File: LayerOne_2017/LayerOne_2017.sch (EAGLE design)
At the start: 102 parts, among them IC1 STM32F446_LQFP64LQFP64, IC2 REG1117, J1 SPI_TFT_DISPLAY, Q1 2N2222, Q2 MMBT2222A, U1 SN65HVD235DR, U2 SN65HVD235DR, U4 SDCARD, U5 FERRITE0805, X1 STEREOJACK, X2 MINI-USB-32005-301

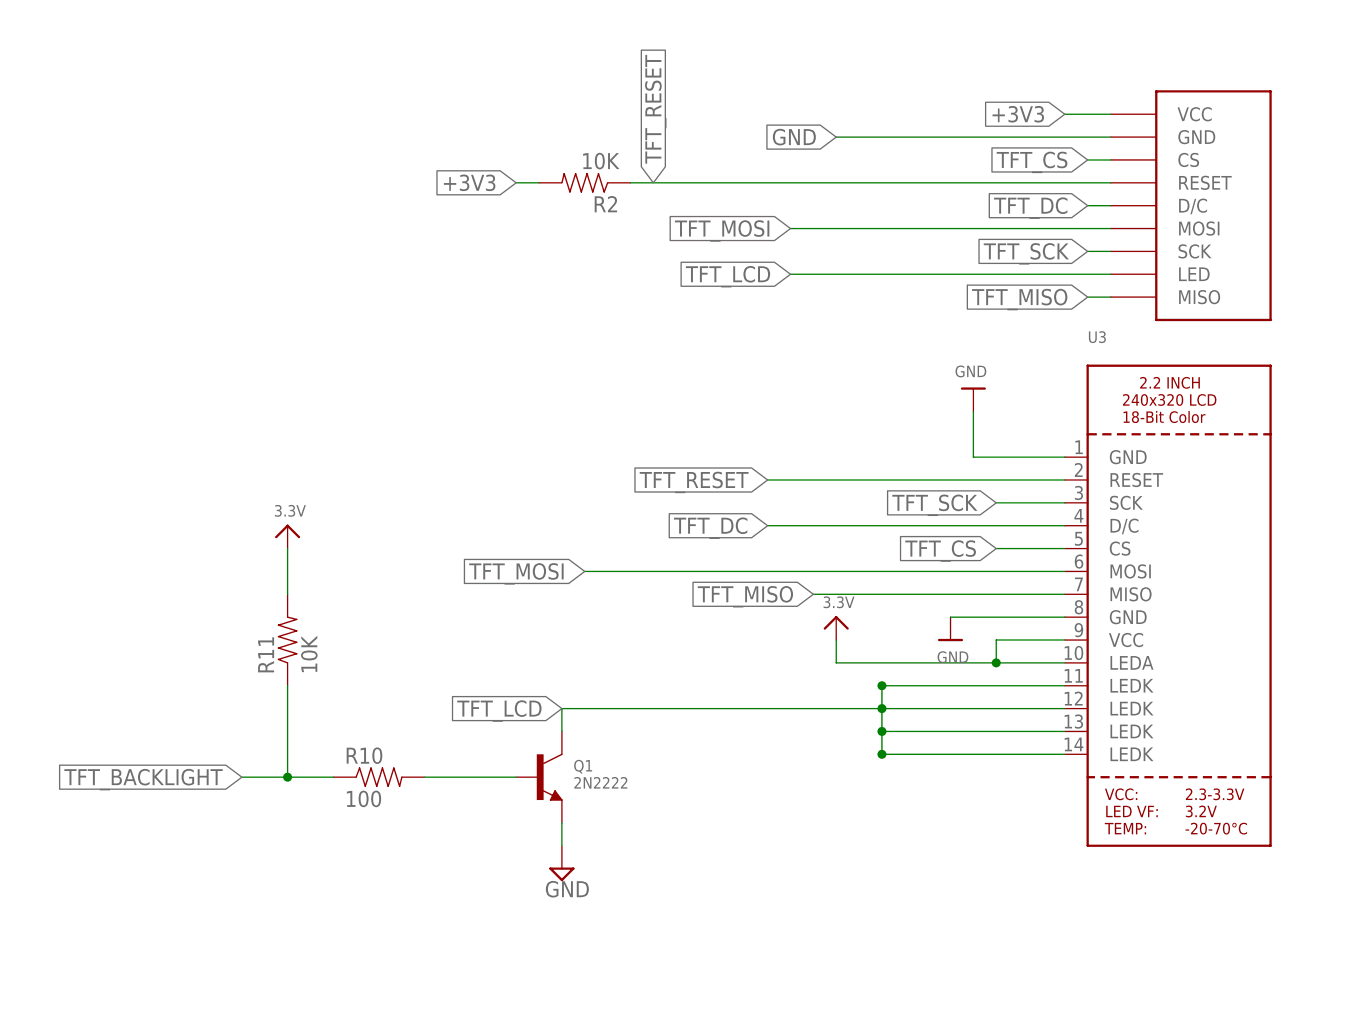
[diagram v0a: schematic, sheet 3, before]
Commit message: 
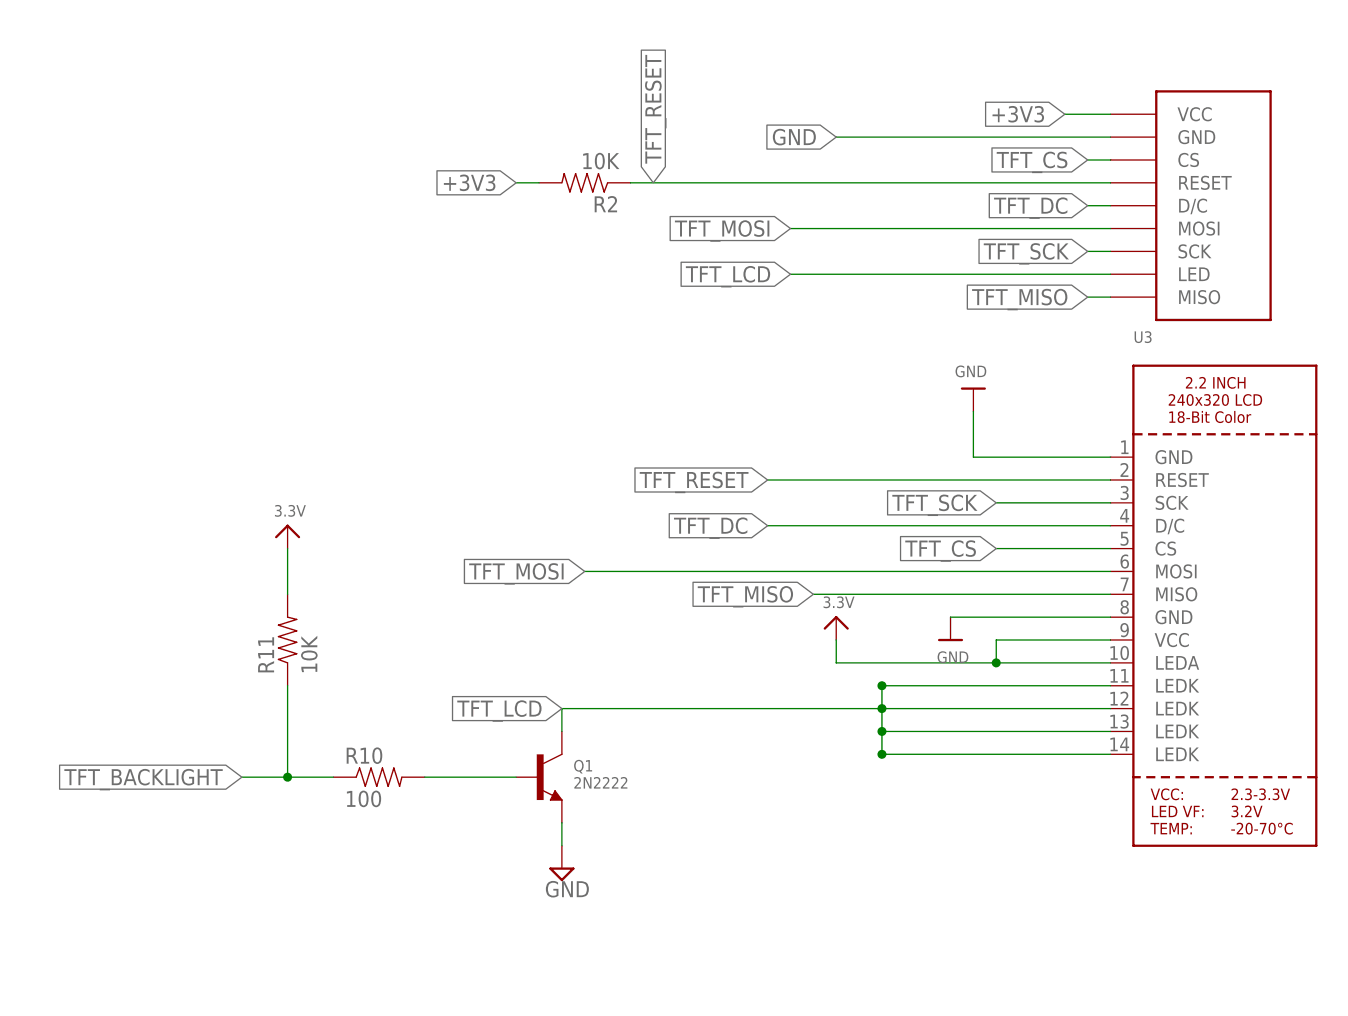
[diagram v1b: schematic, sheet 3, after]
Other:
- note removed: "Connect to MCU"
- moved on the sheet: U3
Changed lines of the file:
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@@
 <instance part="R11" gate="G$1" x="20.32" y="40.64" rot="R90"/>
 <instance part="U$21" gate="G$1" x="20.32" y="53.34"/>
-<instance part="U3" gate="G$1" x="119.38" y="43.18"/>
+<instance part="U3" gate="G$1" x="124.46" y="43.18"/>
 <instance part="U$6" gate="G$1" x="81.28" y="43.18"/>
 <instance part="U$19" gate="G$1" x="93.98" y="40.64"/>
@@
 <segment>
 <pinref part="U3" gate="G$1" pin="GND@2"/>
-<wire x1="106.68" y1="43.18" x2="93.98" y2="43.18" width="0.1524" layer="91"/>
+<wire x1="111.76" y1="43.18" x2="93.98" y2="43.18" width="0.1524" layer="91"/>
 <pinref part="U$19" gate="G$1" pin="GND"/>
 </segment>
@@
 <pinref part="U3" gate="G$1" pin="GND@1"/>
 <pinref part="U$22" gate="G$1" pin="GND"/>
-<wire x1="106.68" y1="60.96" x2="96.52" y2="60.96" width="0.1524" layer="91"/>
+<wire x1="111.76" y1="60.96" x2="96.52" y2="60.96" width="0.1524" layer="91"/>
 <wire x1="96.52" y1="60.96" x2="96.52" y2="66.04" width="0.1524" layer="91"/>
 </segment>
@@
 <pinref part="U3" gate="G$1" pin="LEDA"/>
 <pinref part="U$6" gate="G$1" pin="3.3V"/>
-<wire x1="106.68" y1="38.1" x2="99.06" y2="38.1" width="0.1524" layer="91"/>
+<wire x1="111.76" y1="38.1" x2="99.06" y2="38.1" width="0.1524" layer="91"/>
 <wire x1="99.06" y1="38.1" x2="81.28" y2="38.1" width="0.1524" layer="91"/>
 <wire x1="81.28" y1="38.1" x2="81.28" y2="40.64" width="0.1524" layer="91"/>
 <pinref part="U3" gate="G$1" pin="VCC"/>
-<wire x1="106.68" y1="40.64" x2="99.06" y2="40.64" width="0.1524" layer="91"/>
+<wire x1="111.76" y1="40.64" x2="99.06" y2="40.64" width="0.1524" layer="91"/>
 <wire x1="99.06" y1="40.64" x2="99.06" y2="38.1" width="0.1524" layer="91"/>
 <junction x="99.06" y="38.1"/>
@@
 <net name="TFT_CS" class="0">
 <segment>
-<wire x1="106.68" y1="50.8" x2="99.06" y2="50.8" width="0.1524" layer="91"/>
+<wire x1="111.76" y1="50.8" x2="99.06" y2="50.8" width="0.1524" layer="91"/>
 <label x="99.06" y="50.8" size="1.778" layer="95" rot="R180" xref="yes"/>
 <pinref part="U3" gate="G$1" pin="CS"/>
@@
 <net name="TFT_DC" class="0">
 <segment>
-<wire x1="73.66" y1="53.34" x2="106.68" y2="53.34" width="0.1524" layer="91"/>
+<wire x1="73.66" y1="53.34" x2="111.76" y2="53.34" width="0.1524" layer="91"/>
 <label x="73.66" y="53.34" size="1.778" layer="95" rot="R180" xref="yes"/>
 <pinref part="U3" gate="G$1" pin="D/C"/>
@@
 <net name="TFT_MOSI" class="0">
 <segment>
-<wire x1="106.68" y1="48.26" x2="53.34" y2="48.26" width="0.1524" layer="91"/>
+<wire x1="111.76" y1="48.26" x2="53.34" y2="48.26" width="0.1524" layer="91"/>
 <label x="53.34" y="48.26" size="1.778" layer="95" rot="R180" xref="yes"/>
 <pinref part="U3" gate="G$1" pin="MOSI"/>
@@
 <net name="TFT_SCK" class="0">
 <segment>
-<wire x1="106.68" y1="55.88" x2="99.06" y2="55.88" width="0.1524" layer="91"/>
+<wire x1="111.76" y1="55.88" x2="99.06" y2="55.88" width="0.1524" layer="91"/>
 <label x="99.06" y="55.88" size="1.778" layer="95" rot="R180" xref="yes"/>
 <pinref part="U3" gate="G$1" pin="SCK"/>
@@
 <net name="TFT_MISO" class="0">
 <segment>
-<wire x1="78.74" y1="45.72" x2="106.68" y2="45.72" width="0.1524" layer="91"/>
+<wire x1="78.74" y1="45.72" x2="111.76" y2="45.72" width="0.1524" layer="91"/>
 <label x="78.74" y="45.72" size="1.778" layer="95" rot="R180" xref="yes"/>
 <pinref part="U3" gate="G$1" pin="MISO"/>
@@
 <net name="TFT_RESET" class="0">
 <segment>
-<wire x1="106.68" y1="58.42" x2="73.66" y2="58.42" width="0.1524" layer="91"/>
+<wire x1="111.76" y1="58.42" x2="73.66" y2="58.42" width="0.1524" layer="91"/>
 <label x="73.66" y="58.42" size="1.778" layer="95" rot="R180" xref="yes"/>
 <pinref part="U3" gate="G$1" pin="RESET"/>
@@
 <pinref part="U3" gate="G$1" pin="LEDK@2"/>
 <wire x1="50.8" y1="33.02" x2="86.36" y2="33.02" width="0.1524" layer="91"/>
-<wire x1="86.36" y1="33.02" x2="106.68" y2="33.02" width="0.1524" layer="91"/>
+<wire x1="86.36" y1="33.02" x2="111.76" y2="33.02" width="0.1524" layer="91"/>
 <wire x1="86.36" y1="33.02" x2="86.36" y2="35.56" width="0.1524" layer="91"/>
 <pinref part="U3" gate="G$1" pin="LEDK@4"/>
-<wire x1="106.68" y1="27.94" x2="86.36" y2="27.94" width="0.1524" layer="91"/>
+<wire x1="111.76" y1="27.94" x2="86.36" y2="27.94" width="0.1524" layer="91"/>
 <wire x1="86.36" y1="33.02" x2="86.36" y2="30.48" width="0.1524" layer="91"/>
 <wire x1="86.36" y1="30.48" x2="86.36" y2="27.94" width="0.1524" layer="91"/>
-<wire x1="106.68" y1="30.48" x2="86.36" y2="30.48" width="0.1524" layer="91"/>
+<wire x1="111.76" y1="30.48" x2="86.36" y2="30.48" width="0.1524" layer="91"/>
 <pinref part="U3" gate="G$1" pin="LEDK@3"/>
 <junction x="86.36" y="30.48"/>
 <junction x="86.36" y="33.02"/>
-<wire x1="106.68" y1="35.56" x2="86.36" y2="35.56" width="0.1524" layer="91"/>
+<wire x1="111.76" y1="35.56" x2="86.36" y2="35.56" width="0.1524" layer="91"/>
 <pinref part="U3" gate="G$1" pin="LEDK@1"/>
 <junction x="86.36" y="35.56"/>
@@
 <sheet>
 <plain>
-<text x="93.98" y="-7.62" size="1.778" layer="91" rot="R90">Connect to MCU</text>
 </plain>
 <instances>

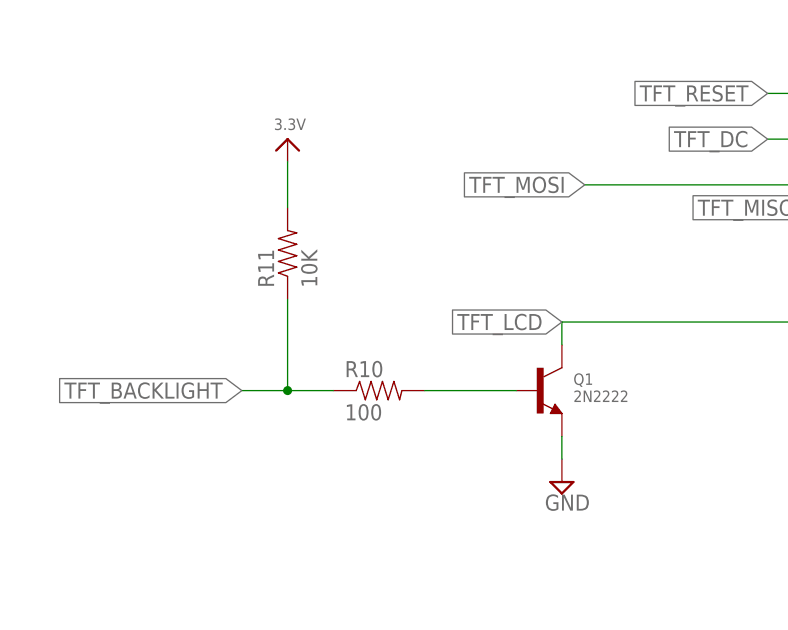
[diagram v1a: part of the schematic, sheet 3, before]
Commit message: Backlight NPN redone
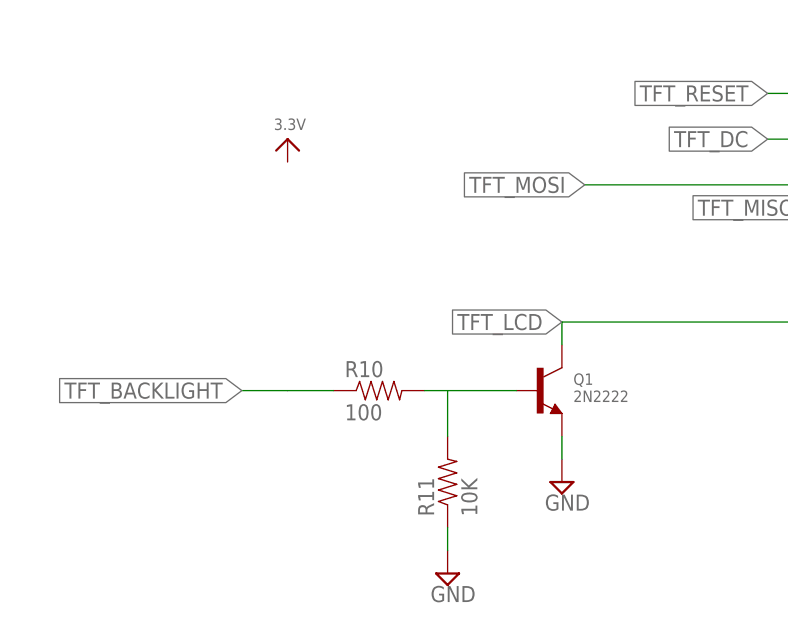
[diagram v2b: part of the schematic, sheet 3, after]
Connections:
- net +3V3: no longer R11.2
- net GND: now also R11.1
- net N$16: now also R11.2
- net TFT_BACKLIGHT: no longer R11.1
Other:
- moved on the sheet: R11
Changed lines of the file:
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@@
 </part>
 <part name="U$43" library="microbuilder" deviceset="GND" device=""/>
+<part name="GND2" library="STM32-PROX" deviceset="GND" device=""/>
 </parts>
 <sheets>
@@
 <instance part="Q1" gate="G$1" x="50.8" y="25.4"/>
 <instance part="R10" gate="G$1" x="30.48" y="25.4"/>
-<instance part="R11" gate="G$1" x="20.32" y="40.64" rot="R90"/>
+<instance part="R11" gate="G$1" x="38.1" y="15.24" rot="R90"/>
 <instance part="U$21" gate="G$1" x="20.32" y="53.34"/>
 <instance part="U3" gate="G$1" x="124.46" y="43.18"/>
@@
 <attribute name="DIGIKEY" x="53.34" y="91.44" size="1.778" layer="96" rot="R180" display="off"/>
 </instance>
+<instance part="GND2" gate="GND" x="38.1" y="5.08"/>
 </instances>
 <busses>
@@
 <wire x1="111.76" y1="96.52" x2="81.28" y2="96.52" width="0.1524" layer="91"/>
 <label x="81.28" y="96.52" size="1.778" layer="95" rot="R180" xref="yes"/>
+</segment>
+<segment>
+<pinref part="GND2" gate="GND" pin="GND"/>
+<pinref part="R11" gate="G$1" pin="1"/>
+<wire x1="38.1" y1="7.62" x2="38.1" y2="10.16" width="0.1524" layer="91"/>
 </segment>
 </net>
@@
 <wire x1="99.06" y1="40.64" x2="99.06" y2="38.1" width="0.1524" layer="91"/>
 <junction x="99.06" y="38.1"/>
-</segment>
-<segment>
-<pinref part="R11" gate="G$1" pin="2"/>
-<pinref part="U$21" gate="G$1" pin="3.3V"/>
-<wire x1="20.32" y1="45.72" x2="20.32" y2="50.8" width="0.1524" layer="91"/>
 </segment>
 <segment>
@@
 <pinref part="R10" gate="G$1" pin="2"/>
 <pinref part="Q1" gate="G$1" pin="B"/>
-<wire x1="35.56" y1="25.4" x2="45.72" y2="25.4" width="0.1524" layer="91"/>
+<wire x1="35.56" y1="25.4" x2="38.1" y2="25.4" width="0.1524" layer="91"/>
+<pinref part="R11" gate="G$1" pin="2"/>
+<wire x1="38.1" y1="25.4" x2="45.72" y2="25.4" width="0.1524" layer="91"/>
+<wire x1="38.1" y1="20.32" x2="38.1" y2="25.4" width="0.1524" layer="91"/>
 </segment>
 </net>
@@
 <wire x1="25.4" y1="25.4" x2="20.32" y2="25.4" width="0.1524" layer="91"/>
 <wire x1="20.32" y1="25.4" x2="15.24" y2="25.4" width="0.1524" layer="91"/>
-<wire x1="20.32" y1="35.56" x2="20.32" y2="25.4" width="0.1524" layer="91"/>
-<junction x="20.32" y="25.4"/>
 <label x="15.24" y="25.4" size="1.778" layer="95" rot="R180" xref="yes"/>
 <pinref part="R10" gate="G$1" pin="1"/>
-<pinref part="R11" gate="G$1" pin="1"/>
-</segment>
-</net>
+</segment>
+</net>

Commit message: Added Power test points
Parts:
- added 3V3, 5V, GND, VBAT, VUSB: PTR1PAD1-13, testpad:PTR1PAD1-13
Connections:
- removed net +3V3: B00T0.2, C10.1, C11.1, C12.1, C13.1, C5.1, C6.1, C7.1, C8.1, C9.1, IC1.VBAT, IC1.VDD@0, IC1.VDD@1, IC1.VDD@2, IC1.VDD@3, IC2.VOUT, J1.VCC, JP1.1, JP4.1, Q2.C, R2.2, R61.2, R62.2, R63.2, R64.2, U1.VDD, U2.VDD, U3.LEDA, U3.VCC, U4.VCC, U5.B
- new net 3V3: 3V3.TP, B00T0.2, C10.1, C11.1, C12.1, C13.1, C5.1, C6.1, C7.1, C8.1, C9.1, IC1.VBAT, IC1.VDD@0, IC1.VDD@1, IC1.VDD@2, IC1.VDD@3, IC2.VOUT, J1.VCC, JP1.1, JP4.1, Q2.C, R2.2, R61.2, R62.2, R63.2, R64.2, U1.VDD, U2.VDD, U3.LEDA, U3.VCC, U4.VCC, U5.B
- net 5V: now also 5V.TP
- net GND: now also GND.TP
- net VBAT: now also VBAT.TP
- net VUSB: now also VUSB.TP
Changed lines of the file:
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@@
 <part name="U$43" library="microbuilder" deviceset="GND" device=""/>
 <part name="GND2" library="STM32-PROX" deviceset="GND" device=""/>
+<part name="VUSB" library="testpad" deviceset="PTR1" device="PAD1-13"/>
+<part name="VBAT" library="testpad" deviceset="PTR1" device="PAD1-13"/>
+<part name="5V" library="testpad" deviceset="PTR1" device="PAD1-13"/>
+<part name="GND" library="testpad" deviceset="PTR1" device="PAD1-13"/>
+<part name="3V3" library="testpad" deviceset="PTR1" device="PAD1-13"/>
 </parts>
 <sheets>
@@
 <instance part="FID2" gate="G$1" x="-116.84" y="106.68"/>
 <instance part="FID3" gate="G$1" x="-116.84" y="101.6"/>
+<instance part="3V3" gate="G$1" x="-88.9" y="101.6" rot="R180"/>
 </instances>
 <busses>
@@
 </segment>
 </net>
-<net name="+3V3" class="0">
+<net name="3V3" class="0">
 <segment>
 <label x="-81.28" y="88.9" size="1.778" layer="95" xref="yes"/>
@@
 <junction x="-88.9" y="88.9"/>
 <wire x1="-83.82" y1="88.9" x2="-81.28" y2="88.9" width="0.1524" layer="91"/>
+<pinref part="3V3" gate="G$1" pin="TP"/>
+<wire x1="-88.9" y1="88.9" x2="-88.9" y2="99.06" width="0.1524" layer="91"/>
 </segment>
 </net>
@@
 </segment>
 </net>
-<net name="+3V3" class="0">
+<net name="3V3" class="0">
 <segment>
 <pinref part="IC1" gate="G$1" pin="VDD@3"/>
@@
 </segment>
 </net>
-<net name="+3V3" class="0">
+<net name="3V3" class="0">
 <segment>
 <pinref part="U3" gate="G$1" pin="LEDA"/>
@@
 </segment>
 </net>
-<net name="+3V3" class="0">
+<net name="3V3" class="0">
 <segment>
 <pinref part="U2" gate="G$1" pin="VDD"/>
@@
 </segment>
 </net>
-<net name="+3V3" class="0">
+<net name="3V3" class="0">
 <segment>
 <pinref part="U4" gate="G$1" pin="VCC"/>
@@
 </instance>
 <instance part="U$43" gate="G$1" x="-58.42" y="-22.86"/>
+<instance part="VUSB" gate="G$1" x="-25.4" y="27.94" rot="R180"/>
+<instance part="VBAT" gate="G$1" x="50.8" y="25.4" rot="R180"/>
 </instances>
 <busses>
@@
 <pinref part="C15" gate="G$1" pin="1"/>
 <wire x1="-12.7" y1="15.24" x2="-22.86" y2="15.24" width="0.1524" layer="91"/>
-<wire x1="-22.86" y1="15.24" x2="-33.02" y2="15.24" width="0.1524" layer="91"/>
+<wire x1="-22.86" y1="15.24" x2="-25.4" y2="15.24" width="0.1524" layer="91"/>
 <label x="-33.02" y="15.24" size="1.778" layer="95"/>
+<pinref part="VUSB" gate="G$1" pin="TP"/>
+<wire x1="-25.4" y1="15.24" x2="-33.02" y2="15.24" width="0.1524" layer="91"/>
+<wire x1="-25.4" y1="15.24" x2="-25.4" y2="25.4" width="0.1524" layer="91"/>
 </segment>
 </net>
@@
 <wire x1="27.94" y1="12.7" x2="38.1" y2="12.7" width="0.1524" layer="91"/>
 <pinref part="U$23" gate="G$1" pin="EN2"/>
-<wire x1="38.1" y1="12.7" x2="58.42" y2="12.7" width="0.1524" layer="91"/>
+<wire x1="38.1" y1="12.7" x2="50.8" y2="12.7" width="0.1524" layer="91"/>
+<wire x1="50.8" y1="12.7" x2="58.42" y2="12.7" width="0.1524" layer="91"/>
 <wire x1="12.7" y1="2.54" x2="38.1" y2="2.54" width="0.1524" layer="91"/>
 <wire x1="38.1" y1="2.54" x2="38.1" y2="12.7" width="0.1524" layer="91"/>
@@
 <wire x1="10.16" y1="45.72" x2="10.16" y2="50.8" width="0.1524" layer="91"/>
 <junction x="10.16" y="50.8"/>
+<pinref part="VBAT" gate="G$1" pin="TP"/>
+<wire x1="50.8" y1="12.7" x2="50.8" y2="22.86" width="0.1524" layer="91"/>
 </segment>
 </net>
@@
 <instance part="U$35" gate="G$1" x="93.98" y="58.42"/>
 <instance part="U$36" gate="G$1" x="109.22" y="73.66"/>
+<instance part="5V" gate="G$1" x="119.38" y="96.52" rot="R180"/>
+<instance part="GND" gate="G$1" x="73.66" y="30.48" rot="R180"/>
 </instances>
 <busses>
@@
 <pinref part="C18" gate="G$1" pin="1"/>
 <wire x1="101.6" y1="86.36" x2="109.22" y2="86.36" width="0.1524" layer="91"/>
-<wire x1="109.22" y1="86.36" x2="124.46" y2="86.36" width="0.1524" layer="91"/>
+<wire x1="109.22" y1="86.36" x2="119.38" y2="86.36" width="0.1524" layer="91"/>
 <junction x="93.98" y="86.36"/>
 <junction x="101.6" y="86.36"/>
 <junction x="109.22" y="86.36"/>
 <label x="124.46" y="88.9" size="1.778" layer="95" rot="R90"/>
+<pinref part="5V" gate="G$1" pin="TP"/>
+<wire x1="119.38" y1="86.36" x2="124.46" y2="86.36" width="0.1524" layer="91"/>
+<wire x1="119.38" y1="93.98" x2="119.38" y2="86.36" width="0.1524" layer="91"/>
 </segment>
 </net>
@@
 <wire x1="60.96" y1="27.94" x2="60.96" y2="25.4" width="0.1524" layer="91"/>
 <pinref part="U$31" gate="G$1" pin="GND"/>
-</segment>
-<segment>
+<wire x1="60.96" y1="25.4" x2="73.66" y2="25.4" width="0.1524" layer="91"/>
+<pinref part="GND" gate="G$1" pin="TP"/>
+<wire x1="73.66" y1="25.4" x2="73.66" y2="27.94" width="0.1524" layer="91"/>
+<junction x="60.96" y="25.4"/>
+</segment>
+<segment>
